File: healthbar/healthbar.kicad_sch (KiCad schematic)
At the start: 57 parts

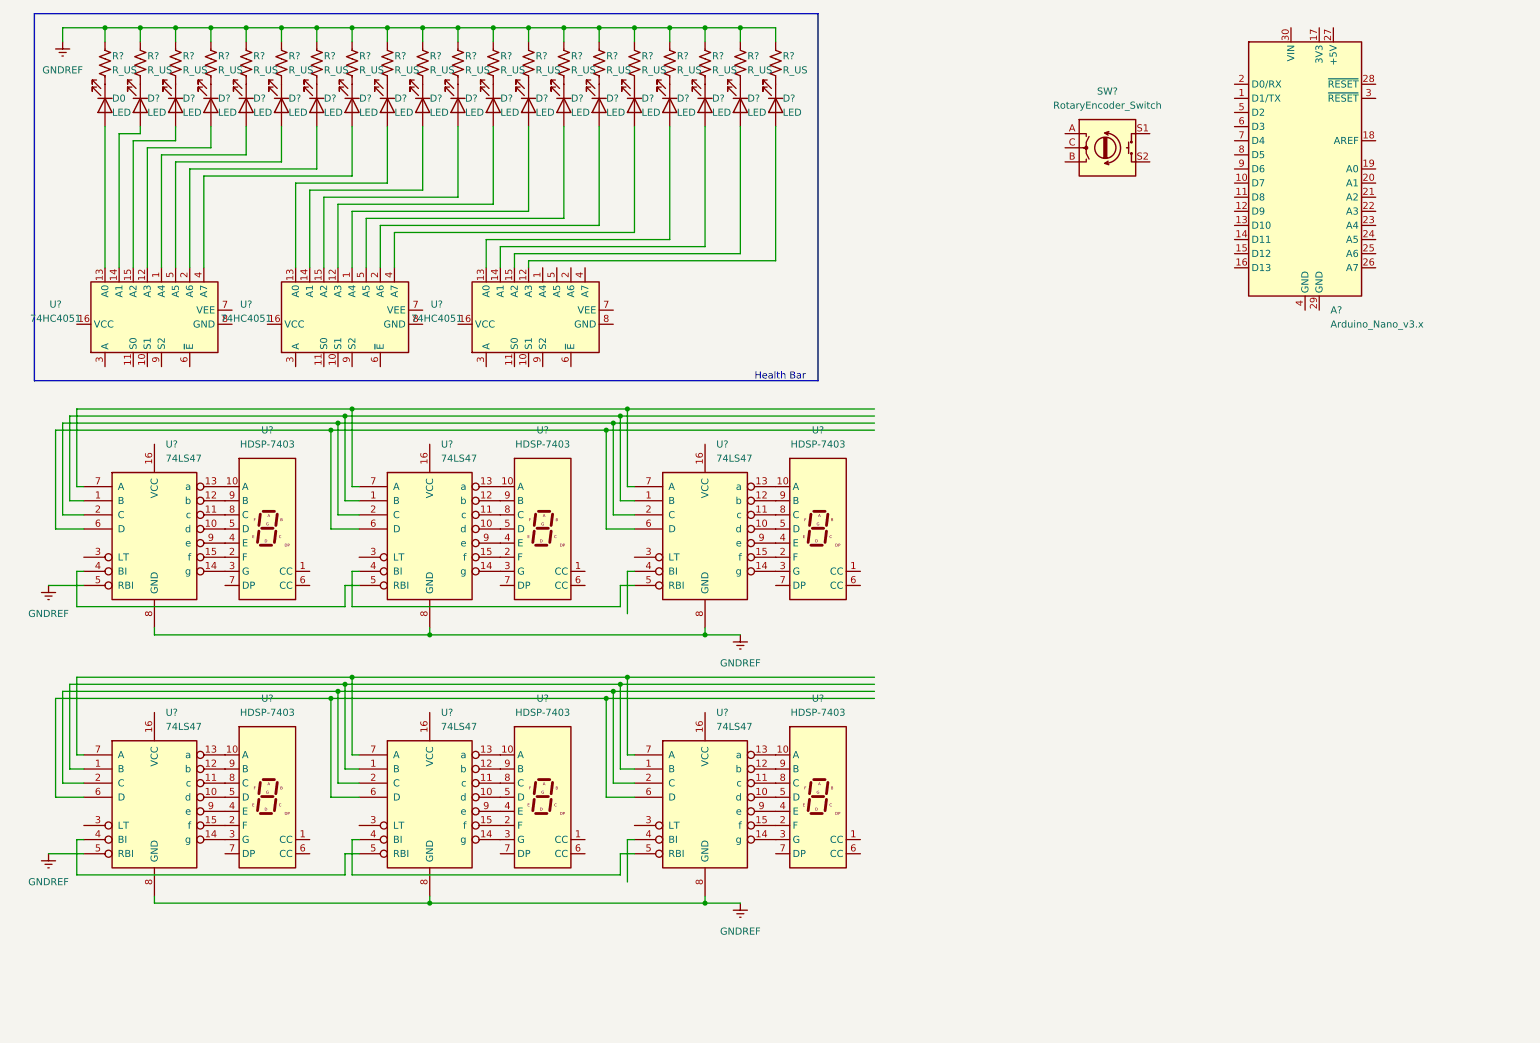
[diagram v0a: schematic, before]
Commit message: circuit done, vcc & gnd needed
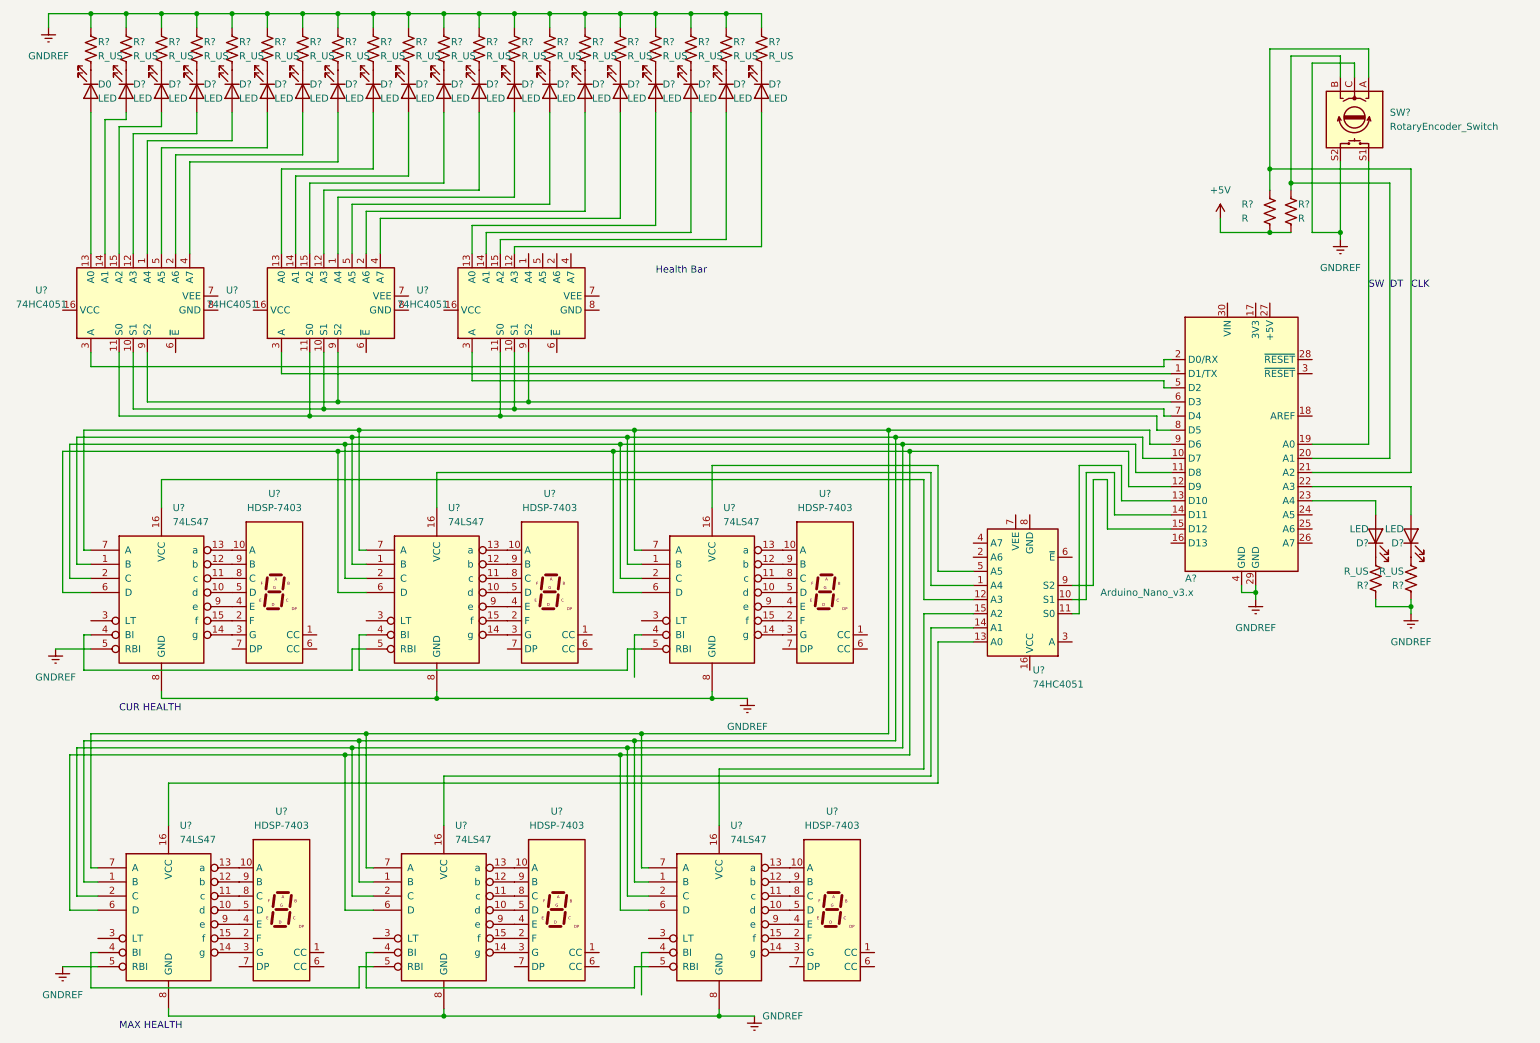
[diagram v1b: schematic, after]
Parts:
- added D? (x2): LED, symbol Device:LED
- added R? (x2): R, symbol Device:R_US
- added R? (x2): R_US, symbol Device:R_US
- added U?: 74HC4051, symbol 74xx:74HC4051
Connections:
- net GNDREF: now also A?.29 (GND), A?.4 (GND), SW?.C, SW?.S2, R?.1, R?.1
- net at U?.10 (S1): now also A?.7 (D4), U?.10 (S1), U?.10 (S1)
- net at U?.11 (S0): now also A?.8 (D5), U?.11 (S0), U?.11 (S0)
- net at U?.3 (A): now also A?.2 (D0/RX)
- net at U?.9 (S2): now also A?.6 (D3), U?.9 (S2), U?.9 (S2)
- net at SW?.A: now also A?.21 (A2), R?.1
- net at SW?.B: now also A?.20 (A1), R?.1
- net at SW?.S1: now also A?.19 (A0)
- net at U?.1 (B), U?.1 (B), U?.1 (B): now also A?.10 (D7), U?.1 (B), U?.1 (B), U?.1 (B)
- net at U?.16 (VCC): now also U?.12 (A3)
- net at U?.2 (C), U?.2 (C), U?.2 (C): now also A?.11 (D8), U?.2 (C), U?.2 (C), U?.2 (C)
- net at U?.6 (D), U?.6 (D), U?.6 (D): now also A?.12 (D9), U?.6 (D), U?.6 (D), U?.6 (D)
- net at U?.7 (A), U?.7 (A), U?.7 (A): now also A?.9 (D6), U?.7 (A), U?.7 (A), U?.7 (A)
- net at U?.16 (VCC): now also U?.14 (A1)
- net at U?.16 (VCC): now also U?.5 (A5)
- net at U?.3 (A): now also A?.1 (D1/TX)
- net at U?.3 (A): now also A?.5 (D2)
- net at U?.16 (VCC): now also U?.1 (A4)
- net at A?.13 (D10): now also U?.11 (S0)
- net at A?.14 (D11): now also U?.10 (S1)
- net at A?.15 (D12): now also U?.9 (S2)
- net at A?.22 (A3): now also D?.2 (A)
- net at A?.23 (A4): now also D?.2 (A)
- net at U?.16 (VCC): now also U?.13 (A0)
- net at U?.16 (VCC): now also U?.15 (A2)
- new net: D?.1 (K), R?.2 (x2)
- new net +5V: R?.2, R?.2
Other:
- note added: "CLK"
- note added: "CUR HEALTH"
- note added: "DT"
- note added: "MAX HEALTH"
- note added: "SW"
- moved on the sheet: A?, D0, D?, R?, SW?, U?

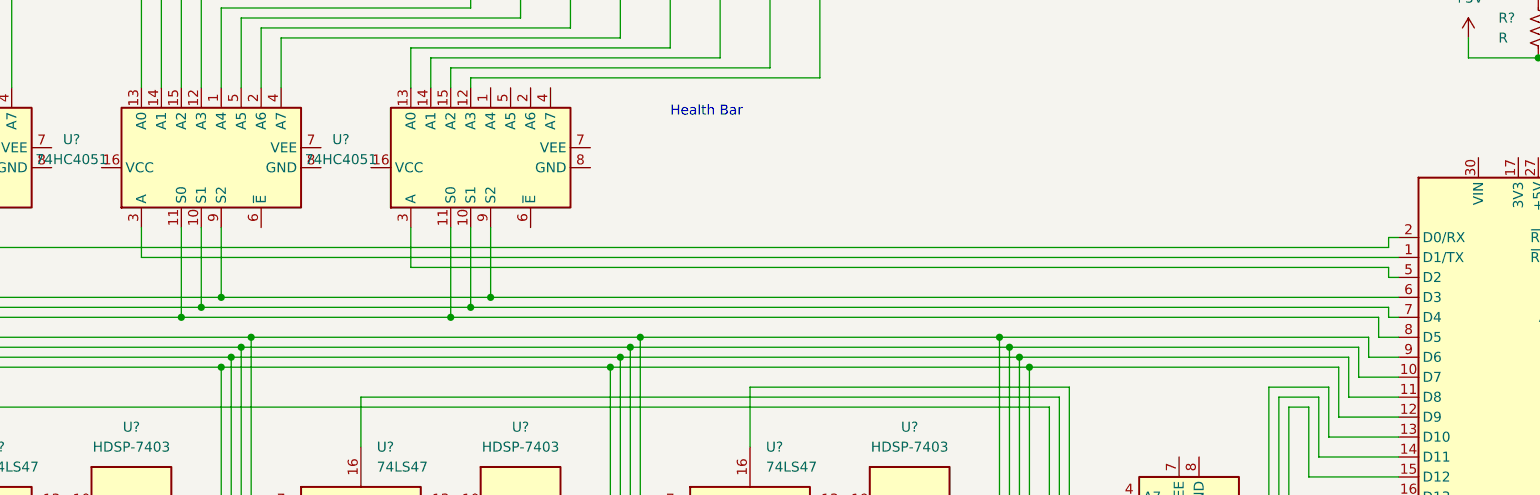
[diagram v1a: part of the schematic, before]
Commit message: Started arduino logic, updated sch d1d0d2
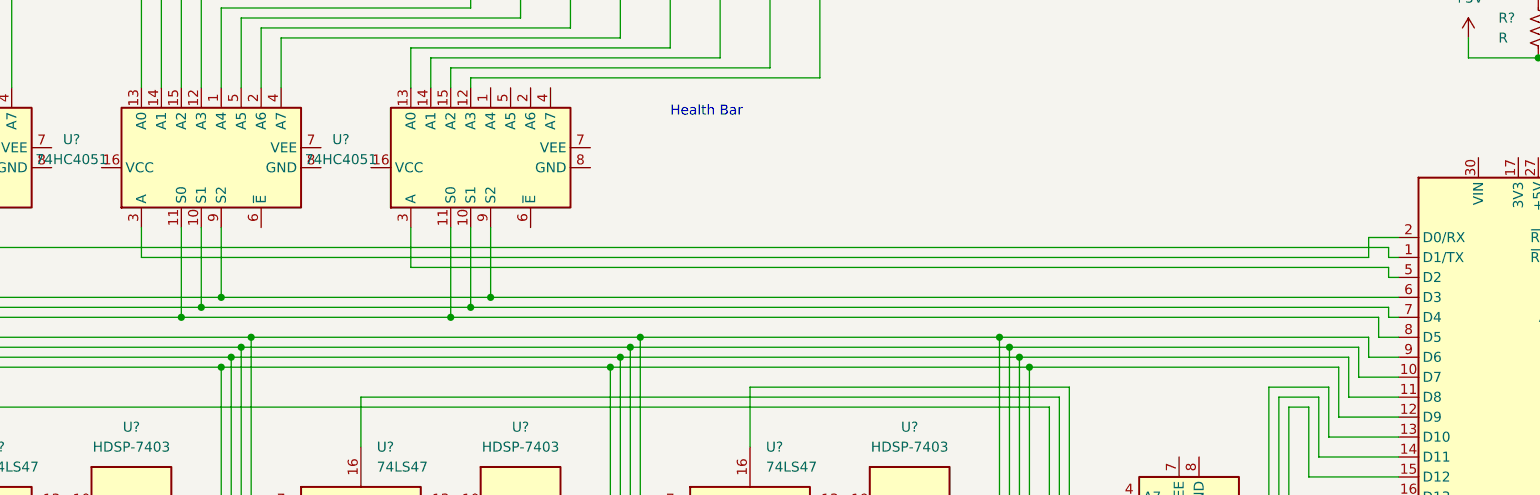
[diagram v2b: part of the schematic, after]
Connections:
- net at U?.3 (A): now also A?.1 (D1/TX); no longer A?.2 (D0/RX)
- net at U?.3 (A): now also A?.2 (D0/RX); no longer A?.1 (D1/TX)
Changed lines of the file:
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@@
+    (stroke (width 0) (type default) (color 0 0 0 0))
+  )
+  (wire (pts (xy 214.63 78.74) (xy 214.63 76.2))
     (stroke (width 0) (type default) (color 0 0 0 0))
   )
@@
     (stroke (width 0) (type default) (color 0 0 0 0))
   )
-  (wire (pts (xy 217.17 76.2) (xy 218.44 76.2))
-    (stroke (width 0) (type default) (color 0 0 0 0))
-  )
   (wire (pts (xy 62.23 13.97) (xy 62.23 16.51))
     (stroke (width 0) (type default) (color 0 0 0 0))
@@
     (stroke (width 0) (type default) (color 0 0 0 0))
   )
+  (wire (pts (xy 217.17 77.47) (xy 217.17 78.74))
+    (stroke (width 0) (type default) (color 0 0 0 0))
+  )
   (wire (pts (xy 63.5 86.36) (xy 97.79 86.36))
     (stroke (width 0) (type default) (color 0 0 0 0))
@@
     (stroke (width 0) (type default) (color 0 0 0 0))
   )
-  (wire (pts (xy 217.17 77.47) (xy 217.17 76.2))
-    (stroke (width 0) (type default) (color 0 0 0 0))
-  )
   (wire (pts (xy 118.11 118.11) (xy 123.19 118.11))
     (stroke (width 0) (type default) (color 0 0 0 0))
@@
     (stroke (width 0) (type default) (color 0 0 0 0))
   )
+  (wire (pts (xy 214.63 76.2) (xy 218.44 76.2))
+    (stroke (width 0) (type default) (color 0 0 0 0))
+  )
   (wire (pts (xy 254 25.4) (xy 254 20.32))
     (stroke (width 0) (type default) (color 0 0 0 0))
@@
     (stroke (width 0) (type default) (color 0 0 0 0))
   )
+  (wire (pts (xy 217.17 78.74) (xy 218.44 78.74))
+    (stroke (width 0) (type default) (color 0 0 0 0))
+  )
   (wire (pts (xy 55.88 13.97) (xy 55.88 16.51))
     (stroke (width 0) (type default) (color 0 0 0 0))
@@
     (stroke (width 0) (type default) (color 0 0 0 0))
   )
-  (wire (pts (xy 58.42 78.74) (xy 218.44 78.74))
-    (stroke (width 0) (type default) (color 0 0 0 0))
-  )
+  (wire (pts (xy 58.42 78.74) (xy 214.63 78.74))
+    (stroke (width 0) (type default) (color 0 0 0 0))
+  )
